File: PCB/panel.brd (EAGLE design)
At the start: 110 x 110 mm, 20 parts, among them U1 22PINHEADER22PINHEADER, U2 22PINHEADER22PINHEADER

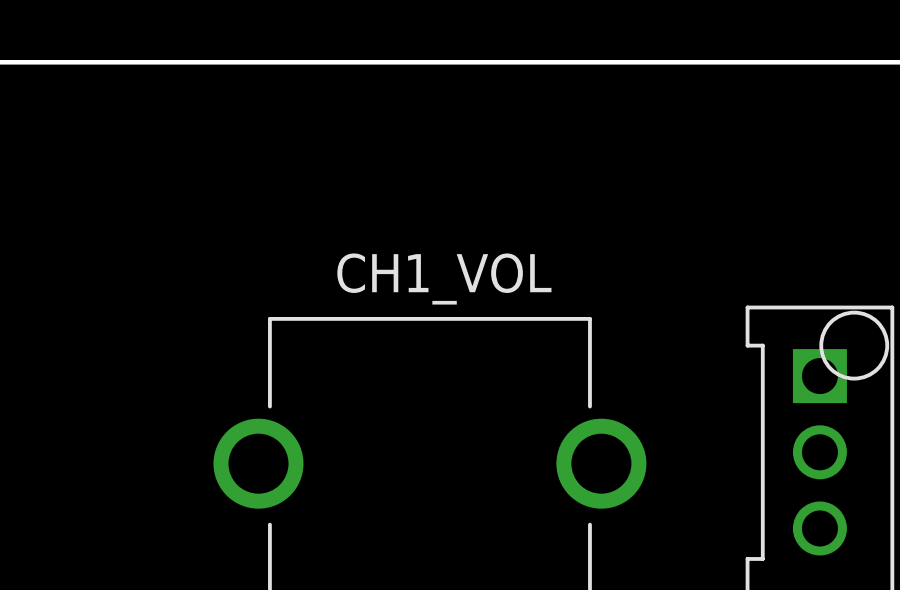
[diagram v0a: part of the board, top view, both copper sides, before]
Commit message: Add switch and analog selectors
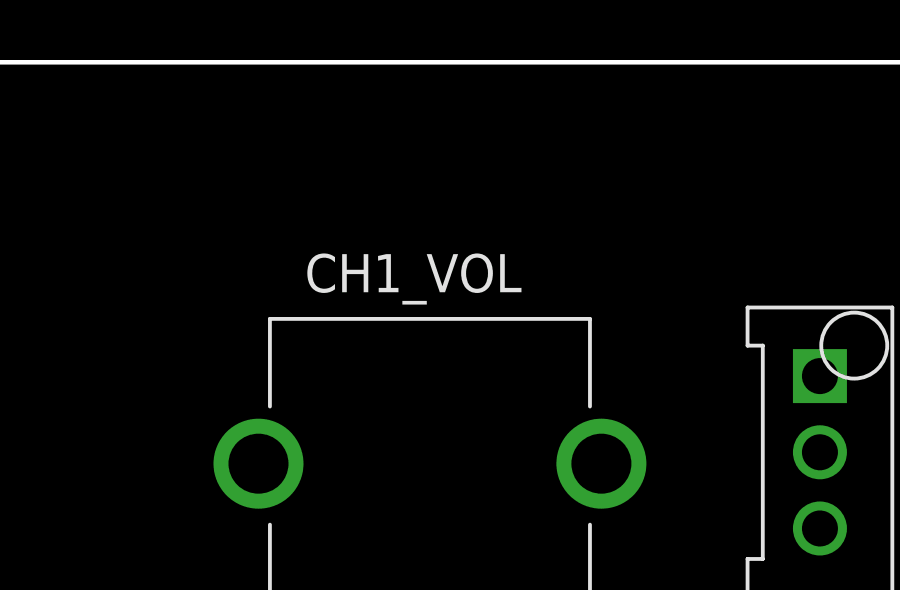
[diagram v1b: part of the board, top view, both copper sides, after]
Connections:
- new net LED_GREEN: U2.22
- new net LED_RED: U2.21
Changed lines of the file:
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@@
 <setting verticaltext="up"/>
 </settings>
-<grid distance="1" unitdist="mm" unit="mm" style="lines" multiple="1" display="yes" altdistance="5" altunitdist="mil" altunit="mil"/>
+<grid distance="5" unitdist="mm" unit="mm" style="lines" multiple="1" display="yes" altdistance="1" altunitdist="mm" altunit="mm"/>
 <layers>
 <layer number="1" name="Top" color="4" fill="1" visible="yes" active="yes"/>
@@
 <layer number="46" name="Milling" color="3" fill="1" visible="no" active="yes"/>
 <layer number="47" name="Measures" color="7" fill="1" visible="no" active="yes"/>
-<layer number="48" name="Document" color="7" fill="1" visible="yes" active="yes"/>
+<layer number="48" name="Document" color="7" fill="1" visible="no" active="yes"/>
 <layer number="49" name="Reference" color="7" fill="1" visible="yes" active="yes"/>
 <layer number="50" name="dxf" color="7" fill="1" visible="no" active="no"/>
@@
 <attribute name="MOUSERNR" value="858-P0915NQC15AR100K" x="8" y="145" size="1.778" layer="27" display="off"/>
 <attribute name="MPN" value="P0915N-QC15AR100K" x="8" y="145" size="1.778" layer="27" display="off"/>
-<attribute name="NAME" x="20.825" y="102.335" size="1.27" layer="21"/>
+<attribute name="NAME" x="19.825" y="102.335" size="1.27" layer="21"/>
 <attribute name="SUPPLIER" value="Mouser" x="8" y="145" size="1.778" layer="27" display="off"/>
 </element>
@@
 <wire x1="83.54" y1="86.46" x2="105.27" y2="62.62" width="0" layer="19" extent="1-1"/>
 </signal>
+<signal name="LED_RED">
+<contactref element="U2" pad="21"/>
+</signal>
+<signal name="LED_GREEN">
+<contactref element="U2" pad="22"/>
+</signal>
 </signals>

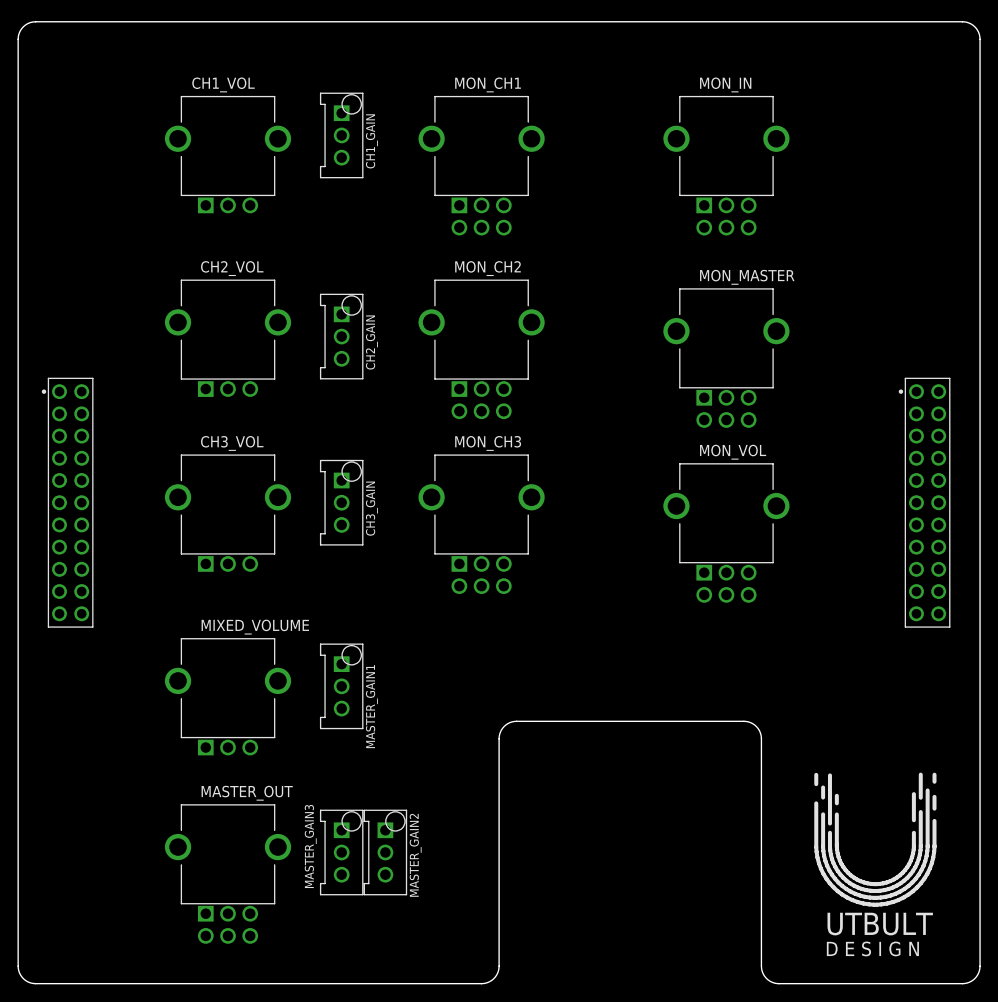
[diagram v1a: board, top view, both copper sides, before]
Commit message: Updating to 2 layer
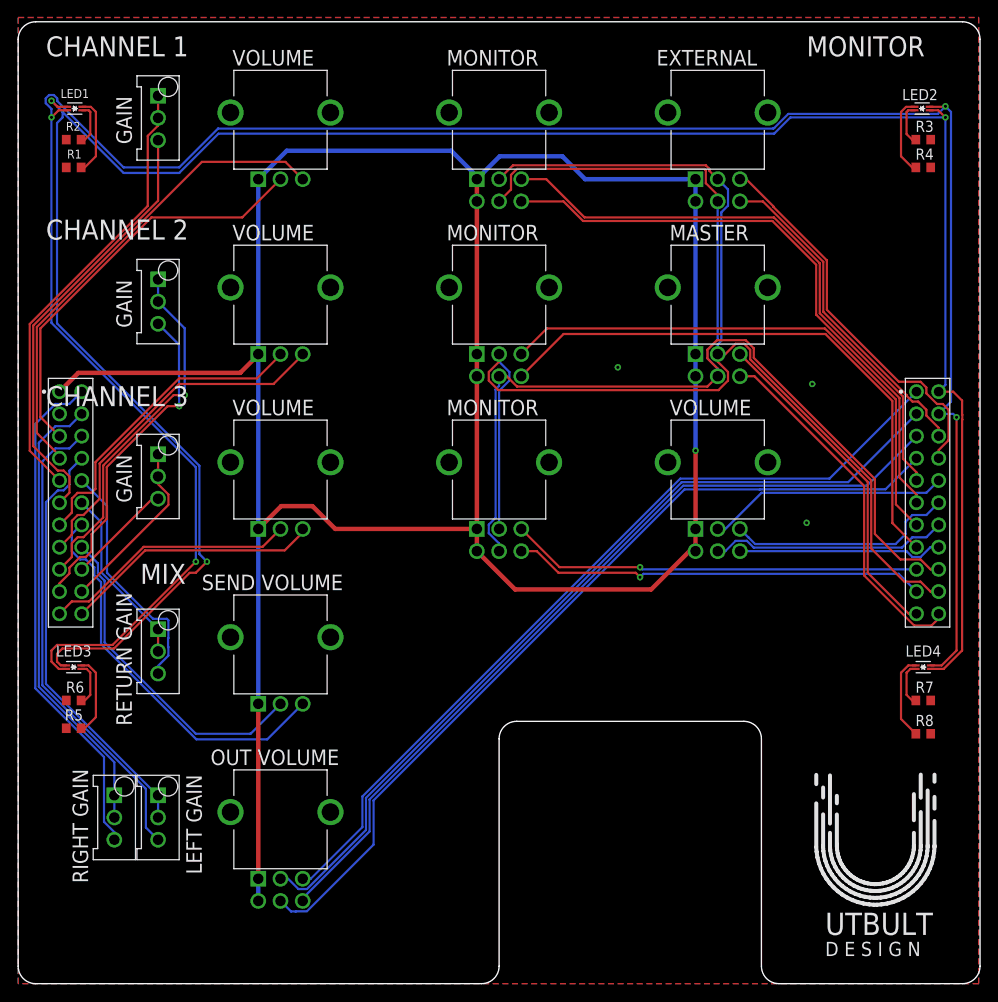
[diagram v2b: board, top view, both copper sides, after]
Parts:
- added LED1, LED2, LED3, LED4: DUAL_LEDDUAL_LED, lib:RESCAXE40P80X160X50-4N
- added R1, R2, R3, R4, R5, R6, R7, R8: 4.7k, lib:R0603
- moved MASTER_GAIN2 26.3 mm to (16.0, 19.0)
- moved MASTER_GAIN3 26.3 mm to (11.0, 19.0)
- moved CH2_GAIN 21.4 mm to (16.0, 78.0)
- moved MASTER_GAIN1 21.4 mm to (16.0, 38.0)
- moved CH3_GAIN 21.2 mm to (16.0, 58.0)
- moved CH1_GAIN 21.1 mm to (16.0, 99.0)
- moved MIXED_VOLUME 7.81 mm to (30.0, 32.0)
- moved CH2_VOL 7.21 mm to (30.0, 72.0)
- moved CH3_VOL 7.21 mm to (30.0, 52.0)
- moved MASTER_OUT 7.21 mm to (30.0, 12.0)
- moved CH1_VOL 6.71 mm to (30.0, 92.0)
- moved MON_MASTER 5.10 mm to (80.0, 72.0)
- moved MON_VOL 5.10 mm to (80.0, 52.0)
- moved MON_CH2 4.47 mm to (55.0, 72.0)
- moved MON_CH3 4.47 mm to (55.0, 52.0)
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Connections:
- new net N$1: LED1.4, R1.1
- new net N$2: LED1.3, R2.1
- new net N$3: LED2.4, R3.1
- new net N$4: LED2.3, R4.1
- new net N$5: LED3.4, R5.1
- new net N$6: LED3.3, R6.1
- new net N$7: LED4.4, R7.1
- new net N$8: LED4.3, R8.1
- net GND: now also R1.2, R2.2, R3.2, R4.2, R5.2, R6.2, R7.2, R8.2
- net LED_GREEN: now also LED1.1, LED2.1, LED3.1, LED4.1
- net LED_RED: now also LED1.2, LED2.2, LED3.2, LED4.2
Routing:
- net VDD: track 0.00 -> 304.6 mm, vias 0 -> 1
- net LED_RED: track 0.00 -> 266.3 mm, vias 0 -> 4
- net LED_GREEN: track 0.00 -> 262.8 mm, vias 0 -> 3
- net MONITOR_MIX_R: track 0.00 -> 146.4 mm
- net MONITOR_MIX_L: track 0.00 -> 143.9 mm
- net MASTER_VOLUME2_P2: track 0.00 -> 97.9 mm
- net MASTER_VOLUME2_P5: track 0.00 -> 97.7 mm
- net MASTER_VOLUME2_P3: track 0.00 -> 95.3 mm
- net MASTER_VOLUME2_P6: track 0.00 -> 94.5 mm
- net MONITOR_VOLUME1_P3: track 0.00 -> 68.7 mm
- net MONITOR_VOLUME1_P6: track 0.00 -> 67.5 mm
- net MONITOR_VOLUME2_P3: track 0.00 -> 65.5 mm
- net MONITOR_VOLUME2_P6: track 0.00 -> 62.7 mm
- net GAIN3_P3: track 0.00 -> 58.1 mm
- net VOL1_P3_CH1: track 0.00 -> 55.1 mm
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- added copper zone on layer 1, net GND
- added copper zone on layer 16, net GND
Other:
- board text added: "CHANNEL 1"
- board text added: "CHANNEL 2"
- board text added: "CHANNEL 3"
- board text added: "EXTERNAL"
- board text added: "GAIN"
- board text added: "LEFT GAIN"
- board text added: "MASTER"
- board text added: "MIX"
- board text added: "MONITOR"
- board text added: "OUT VOLUME"
- board text added: "RETURN GAIN"
- board text added: "RIGHT GAIN"
- board text added: "SEND VOLUME"
- board text added: "VOLUME"
